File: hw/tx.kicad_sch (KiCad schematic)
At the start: 35 parts, among them T301 BN-43-202_DualPri_CTSec, U301 ICE40UP5K-SG48ITR, Y301 40MHz

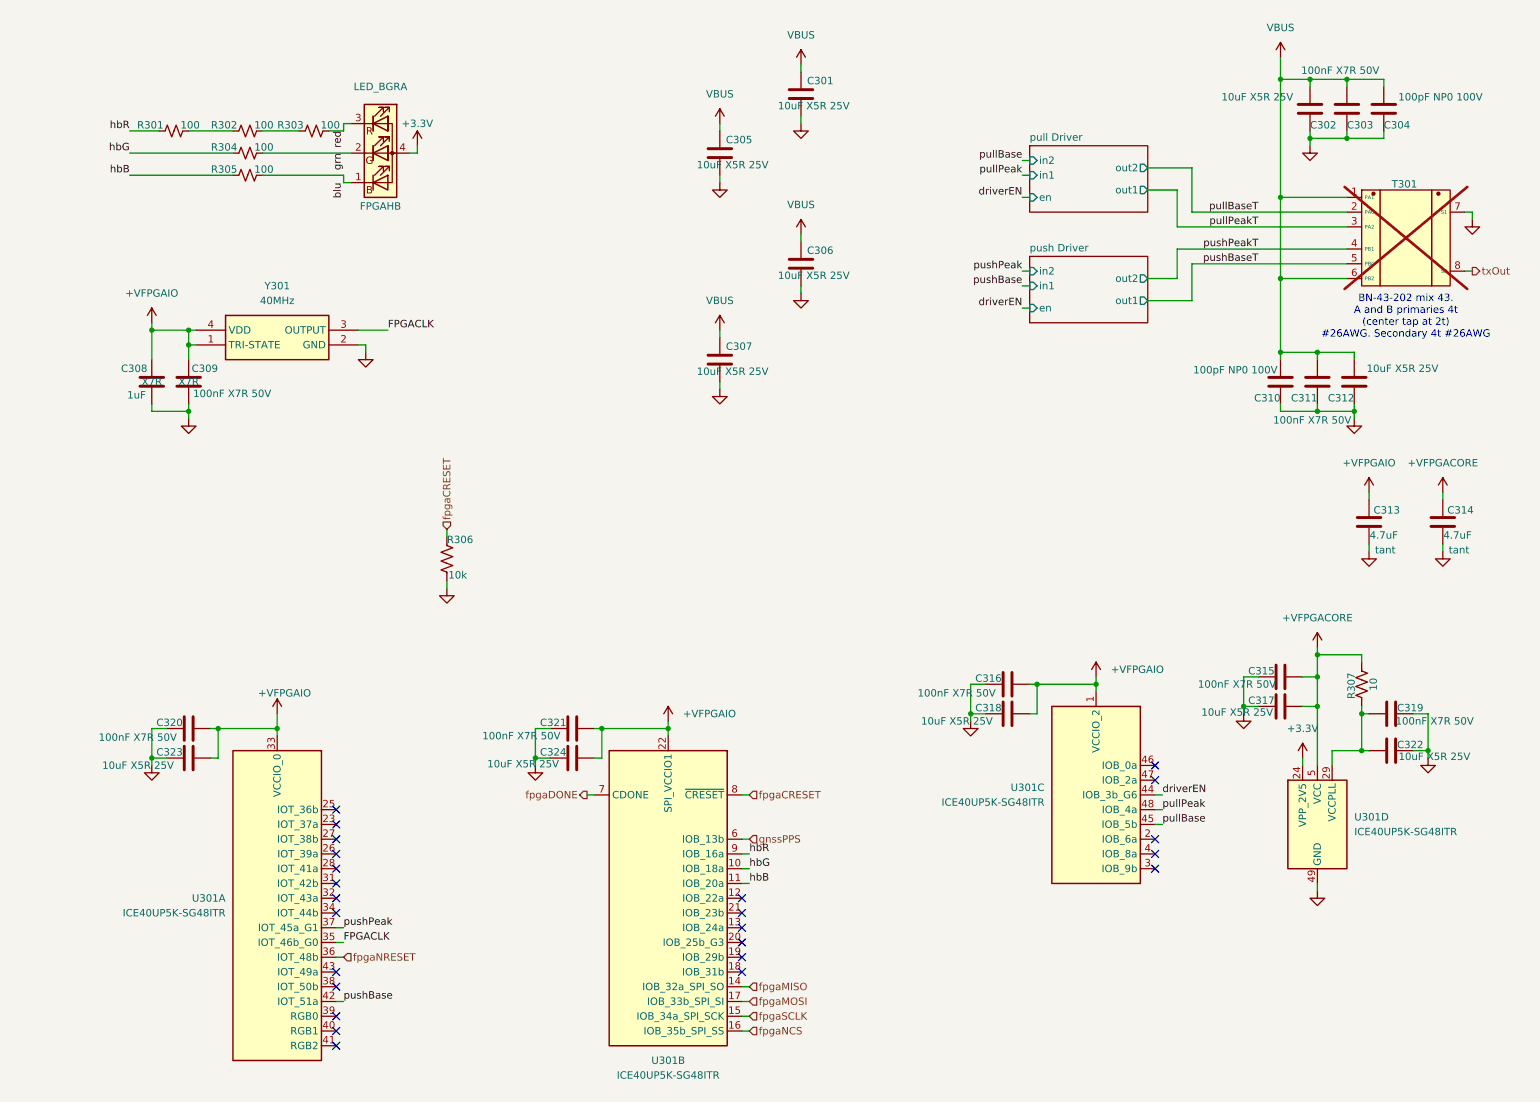
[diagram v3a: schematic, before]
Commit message: Add symbols for new components, switch to SI5351 in place of FPGA. Simplify!
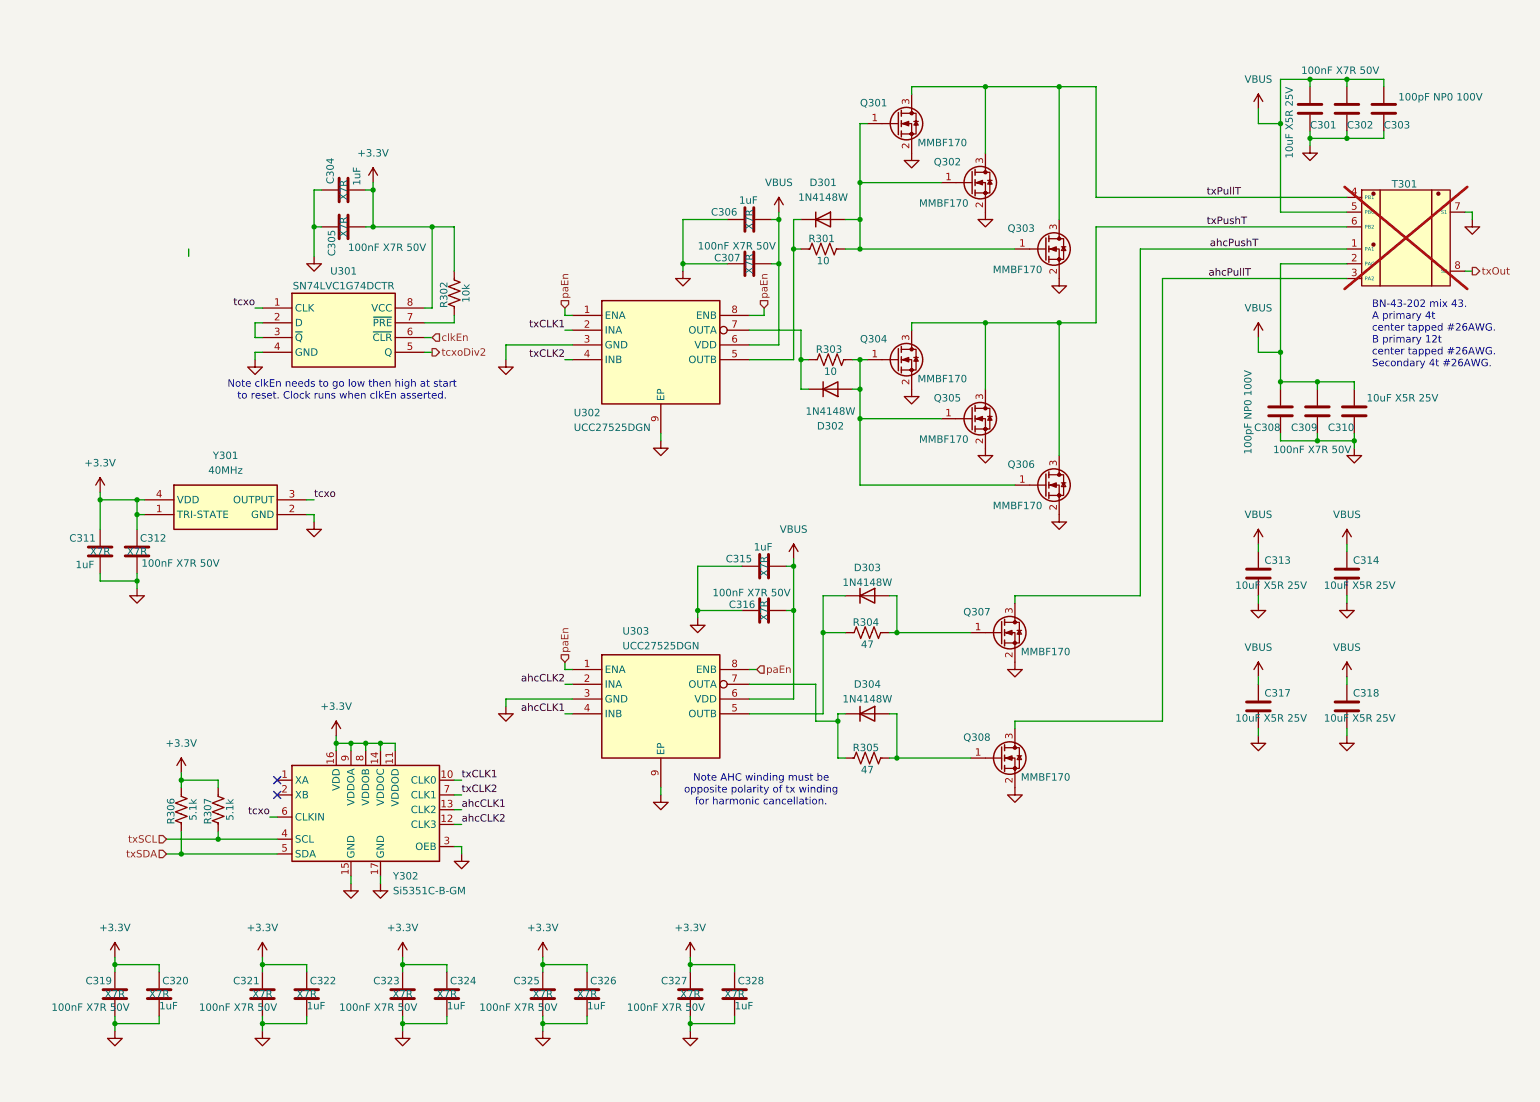
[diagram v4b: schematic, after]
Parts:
- removed C313, C314: 4.7uF, Capacitor_SMD:C_0402_1005Metric, symbol Device:C
- removed C317, C318: 10uF X5R 25V, Capacitor_SMD:C_0603_1608Metric, symbol Device:C
- removed D301: LED_BGRA, Library:UHD111AFKAC3K23E1L3VG5ZB3Z3, symbol Device:LED_BGRA
- removed R301, R302, R303, R304, R305: 100, Resistor_SMD:R_0402_1005Metric, symbol Device:R_Small_US
- removed U301: ICE40UP5K-SG48ITR, Package_DFN_QFN:QFN-48-1EP_7x7mm_P0.5mm_EP5.6x5.6mm, symbol FPGA_Lattice:ICE40UP5K-SG48ITR
- added C304, C306, C326, C328: 1uF, Capacitor_SMD:C_0402_1005Metric, symbol Device:C
- added C305, C307, C325, C327: 100nF X7R 50V, Capacitor_SMD:C_0603_1608Metric, symbol Device:C
- added D301, D302, D303, D304: 1N4148W, Diode_SMD:D_SOD-123, symbol Diode:1N4148W
- added Q301, Q302, Q303, Q304, Q305, Q306, Q307, Q308: MMBF170, Package_TO_SOT_SMD:SOT-23, symbol Transistor_FET:BS170F
- added R301, R303: 10, Resistor_SMD:R_0603_1608Metric, symbol Device:R_US
- added R302: 10k, Resistor_SMD:R_0603_1608Metric, symbol Device:R_US
- added R304, R305: 47, Resistor_SMD:R_0603_1608Metric, symbol Device:R_US
- added U301: SN74LVC1G74DCTR, Library:SOP65P400X130-8N, symbol Library:SN74LVC1G74DCTR
- added U302, U303: UCC27525DGN, Library:SOP65P490X110-9N, symbol Library:UCC27525DGN
- added Y302: Si5351C-B-GM, Library:QFN50P300X300X90-17N-D, symbol Library:Si5351C-B-GM1
- C315, C320: value 100nF X7R 50V -> 1uF; footprint Capacitor_SMD:C_0603_1608Metric -> Capacitor_SMD:C_0402_1005Metric; LCSC C24452 -> C14445; LCSC_PN (none) -> C301928; MFG Kyocera AVX -> muRata; MPN KGM15BR71H104KT -> GRM155Z71A105KE1D; Manufacturer (none) -> Murata; Mouser_PN 581-KGM15BR71H104KT -> 81-GRM155Z71A105KE1D; working-voltage 50V -> 10V
- C322, C324: value 10uF X5R 25V -> 1uF; footprint Capacitor_SMD:C_0603_1608Metric -> Capacitor_SMD:C_0402_1005Metric; LCSC C96446 -> C14445; LCSC_PN (none) -> C301928; MFG Kyocera AVX -> muRata; MPN CM105X5R106M25AT -> GRM155Z71A105KE1D; Manufacturer (none) -> Murata; Mouser_PN 346-CM105X5R106M25AT -> 81-GRM155Z71A105KE1D; cap-type (none) -> X7R; working-voltage 25V -> 10V
- C323: value 10uF X5R 25V -> 100nF X7R 50V; LCSC C96446 -> C24452; MPN CM105X5R106M25AT -> KGM15BR71H104KT; Mouser_PN 346-CM105X5R106M25AT -> 581-KGM15BR71H104KT; cap-type (none) -> X7R; working-voltage 25V -> 50V
- R306: value 10k -> 5.1k; footprint Resistor_SMD:R_0402_1005Metric -> Resistor_SMD:R_0603_1608Metric; LCSC C60490 -> C2907091; MFG Bourns -> Vishay; MPN CRT0402-FZ-1003GLF -> MCT06030C1009FP500; Mouser_PN 652-CRT0402FZ1003GLF -> 594-MCT06030C1009FP5
- R307: value 10 -> 5.1k
- T301: footprint Library:bn-43-202-horizontal -> Transformer_THT:BN-43-202_Horizontal
- renumbered C302 to C301, C303 to C302, C304 to C303, C310 to C308, C311 to C309, C312 to C310, C308 to C311, C309 to C312, C305 to C313, C301 to C314, C307 to C317, C306 to C318
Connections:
- net pullBaseT is gone; now on net VBUS: T301.2 (PAC)
- net pushBaseT is gone; now on net VBUS: T301.5 (PBC)
- net +3.3V: now also C311.1, C312.1, C319.1, C320.1, C321.1, C322.1, C323.1, C324.1, R306.2, R307.2, Y301.1 (TRI-STATE), Y301.4 (VDD), C304.1, C305.1, C325.1, C326.1, C327.1, C328.1, R302.2, U301.8 (VCC), Y302.11 (VDDOD), Y302.14 (VDDOC), Y302.16 (VDD), Y302.8 (VDDOB), Y302.9 (VDDOA)
- net GND: now also C319.2, C320.2, C321.2, C322.2, C323.2, C324.2, C304.2, C305.2, C306.1, C307.1, C325.2, C326.2, C327.2, C328.2, Q301.2 (S), Q302.2 (S), Q303.2 (S), Q304.2 (S), Q305.2 (S), Q306.2 (S), Q307.2 (S), Q308.2 (S), U301.4 (GND), U302.3 (GND), U302.9 (EP), U303.3 (GND), U303.9 (EP), Y302.15 (GND), Y302.17 (GND), Y302.3 (OEB); no longer C319.1, C320.1, C321.1, C322.1, C323.1, C324.1, R306.2
- net VBUS: now also C315.2, C316.2, C306.2, C307.2, U302.6 (VDD), U303.6 (VDD); no longer T301.1 (PA1), T301.6 (PB2)
- removed net +VFPGACORE: C315.2, R307.2
- removed net +VFPGAIO: C311.1, C312.1, C316.2, C320.2, C321.2, C323.2, C324.2, Y301.1 (TRI-STATE), Y301.4 (VDD)
- net FPGACLK renamed tcxo
- net tcxo: now also U301.1 (CLK), Y302.6 (CLKIN)
- net fpgaCRESET renamed txSDA
- net txSDA: now also Y302.5 (SDA)
- net pullPeakT renamed ahcPullT
- net ahcPullT: now also Q308.3 (D)
- net pushPeakT renamed txPullT
- net txPullT: now also Q301.3 (D), Q302.3 (D), Q303.3 (D)
- new net: D302.2 (A), Q304.1 (G), Q305.1 (G), Q306.1 (G), R303.2
- new net: D303.1 (K), R304.1, U303.5 (OUTB)
- new net: D303.2 (A), Q307.1 (G), R304.2
- new net: D301.2 (A), Q301.1 (G), Q302.1 (G), Q303.1 (G), R301.2
- new net: D301.1 (K), R301.1, U302.5 (OUTB)
- new net: D304.2 (A), Q308.1 (G), R305.2
- new net: D304.1 (K), R305.1, U303.7 (OUTA)
- new net: R302.1, U301.7 (~{PRE})
- new net: D302.1 (K), R303.1, U302.7 (OUTA)
- new net: U301.2 (D), U301.3 (~{Q})
- new net ahcCLK1: U303.4 (INB), Y302.13 (CLK2)
- new net ahcCLK2: U303.2 (INA), Y302.12 (CLK3)
- new net ahcPushT: Q307.3 (D), T301.1 (PA1)
- new net clkEn: U301.6 (~{CLR})
- new net paEn: U302.1 (ENA), U302.8 (ENB), U303.1 (ENA), U303.8 (ENB)
- new net tcxoDiv2: U301.5 (Q)
- new net txCLK1: U302.2 (INA), Y302.10 (CLK0)
- new net txCLK2: U302.4 (INB), Y302.7 (CLK1)
- new net txPushT: Q304.3 (D), Q305.3 (D), Q306.3 (D), T301.6 (PB2)
- new net txSCL: R307.1, Y302.4 (SCL)
- no-connect marks 24 -> 2
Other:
- removed sheet pull Driver
- removed sheet push Driver
- note added: "BN-43-202 mix 43. A primary 4t center tapped #26AWG. B primary 12t center tapped #26AWG. Secondary 4t #26AWG."
- note added: "Note AHC winding must be opposite polarity of tx winding for harmonic cancellation."
- note added: "Note clkEn needs to go low then high at start to reset. Clock runs when clkEn asserted."
- note removed: "BN-43-202 mix 43. A and B primaries 4t (center tap at 2t) #26AWG. Secondary 4t #26AWG"
- title: (none) -> Transmitter
- moved on the sheet: C308, C309, C310, C311, C312, C313, C314, C317, C318, Y301

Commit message: Switch to SI5351C-B-GM for exciter + AHC to attenuate 3rd harmonic on a separate winding on the binocular transformer. Do so layout tweaks. This is much simpler than the FPGA version.
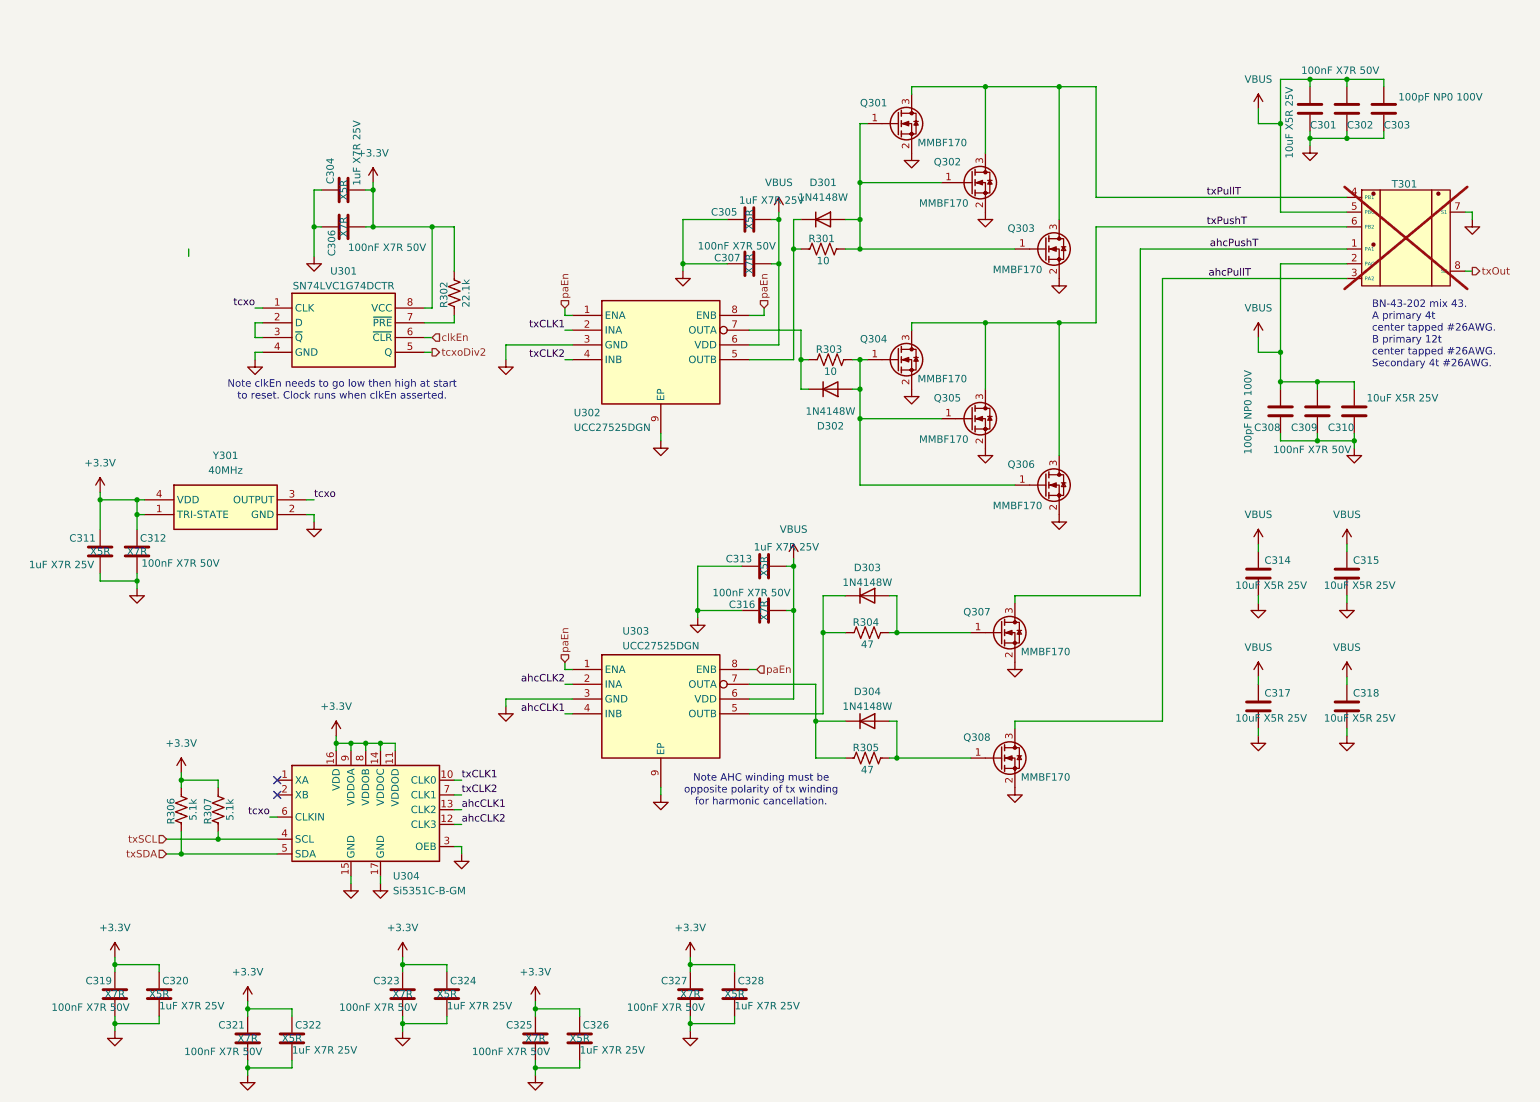
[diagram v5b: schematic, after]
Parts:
- C304, C311, C320, C322, C324, C326, C328: value 1uF -> 1uF X7R 25V; MFG muRata -> Kyocera AVX; MPN GRM155Z71A105KE1D -> 04023D105MAT2A; Mouser_PN 81-GRM155Z71A105KE1D -> 581-04023D105MAT2A; cap-type X7R -> X5R; working-voltage 10V -> 25V
- C305: renamed from C306; value 1uF -> 1uF X7R 25V; MFG muRata -> Kyocera AVX; MPN GRM155Z71A105KE1D -> 04023D105MAT2A; Mouser_PN 81-GRM155Z71A105KE1D -> 581-04023D105MAT2A; cap-type X7R -> X5R; working-voltage 10V -> 25V
- C313: renamed from C315; value 1uF -> 1uF X7R 25V; MFG muRata -> Kyocera AVX; MPN GRM155Z71A105KE1D -> 04023D105MAT2A; Mouser_PN 81-GRM155Z71A105KE1D -> 581-04023D105MAT2A; cap-type X7R -> X5R; working-voltage 10V -> 25V
- R302: value 10k -> 22.1k; footprint Resistor_SMD:R_0603_1608Metric -> Resistor_SMD:R_0402_1005Metric; MFG Vishay -> Yageo; MPN MCT06030C1009FP500 -> RT0402FRD0722K1L; Mouser_PN 594-MCT06030C1009FP5 -> 603-RT0402FRD0722K1L
- R304, R305: footprint Resistor_SMD:R_0603_1608Metric -> Resistor_SMD:R_0402_1005Metric; MFG Vishay -> Yageo; MPN MCT06030C1009FP500 -> AC0402FR-0747RL; Mouser_PN 594-MCT06030C1009FP5 -> 603-AC0402FR-0747RL
- R306, R307: footprint Resistor_SMD:R_0603_1608Metric -> Resistor_SMD:R_0402_1005Metric; MPN MCT06030C1009FP500 -> MCS04020C5101FE000; Mouser_PN 594-MCT06030C1009FP5 -> 594-MCS04020C5101FE0
- T301: footprint Transformer_THT:BN-43-202_Horizontal -> Library:bn-43-202-horizontal
- renumbered C305 to C306, C313 to C314, C314 to C315, Y302 to U304
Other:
- moved on the sheet: C321, C322, C325, C326, D304
